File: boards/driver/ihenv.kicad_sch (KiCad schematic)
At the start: 8 parts, among them Q56 MMBT2222, Q57 MMBT2907, Q58 MMBT2222

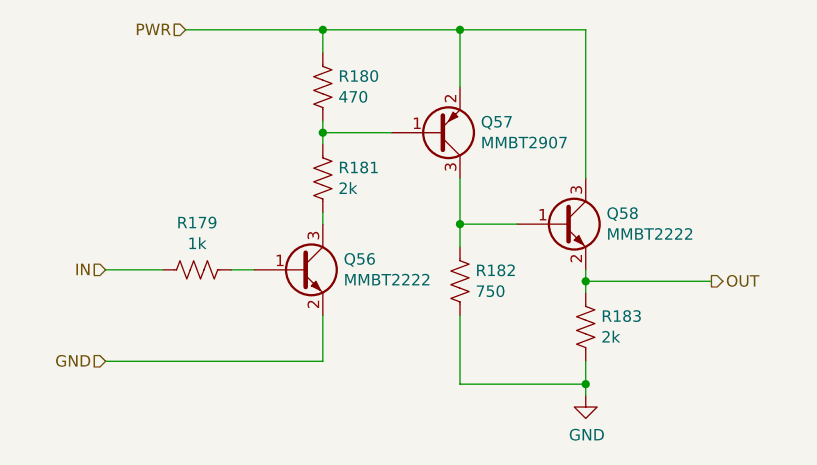
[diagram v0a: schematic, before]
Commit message: Driver: Added a 5V->3.3V LDO to replace the reversed cmod header, added jumpers for the 200R parallel returns, and renamed subcircuit ports to avoid unexpected ground connections.
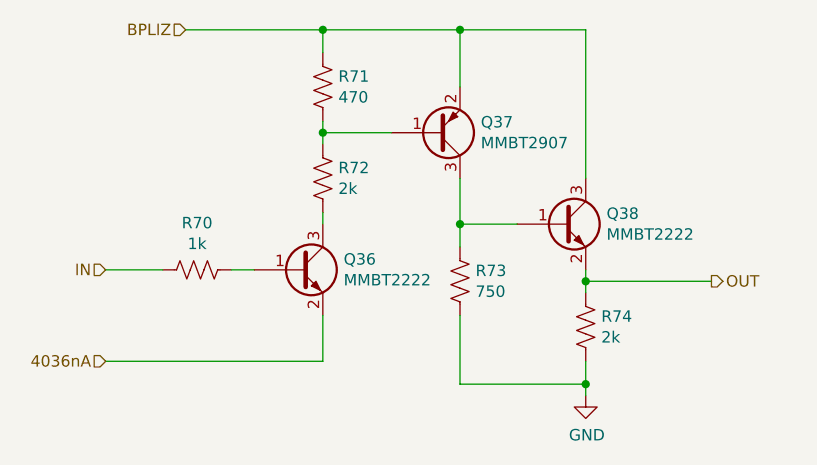
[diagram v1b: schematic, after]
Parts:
- renumbered Q56 to Q36, Q57 to Q37, Q58 to Q38, R179 to R70, R180 to R71, R181 to R72, R182 to R73, R183 to R74
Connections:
- net GND: no longer Q36.2 (E)
- net PWR renamed BPLIZ
- new net 4036nA: Q36.2 (E)
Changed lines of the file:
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@@
     (stroke (width 0) (type default) (color 0 0 0 0))
   )
-  (hierarchical_label "GND" (shape input) (at 90.17 102.87 180)
+  (hierarchical_label "4036nA" (shape input) (at 90.17 102.87 180)
     (effects (font (size 1.27 1.27)) (justify right))
   )
@@
     (effects (font (size 1.27 1.27)) (justify right))
   )
-  (hierarchical_label "PWR" (shape input) (at 99.06 66.04 180)
+  (hierarchical_label "BPLIZ" (shape input) (at 99.06 66.04 180)
     (effects (font (size 1.27 1.27)) (justify right))
   )
   (symbol (lib_id "Device:R_US") (at 100.33 92.71 270)
     (in_bom yes) (on_board yes)
-    (property "Reference" "R179" (id 0) (at 100.33 87.503 90))
+    (property "Reference" "R70" (id 0) (at 100.33 87.503 90))
     (property "Value" "1k" (id 1) (at 100.33 89.8144 90))
     (property "Footprint" "Resistor_SMD:R_0603_1608Metric" (id 2) (at 100.076 93.726 90)
@@
   (symbol (lib_id "Device:Q_NPN_BEC") (at 111.76 92.71 0)
     (in_bom yes) (on_board yes)
-    (property "Reference" "Q56" (id 0) (at 116.6114 91.5416 0)
+    (property "Reference" "Q36" (id 0) (at 116.6114 91.5416 0)
       (effects (font (size 1.27 1.27)) (justify left))
     )
@@
   (symbol (lib_id "Device:Q_PNP_BEC") (at 127 77.47 0) (mirror x)
     (in_bom yes) (on_board yes)
-    (property "Reference" "Q57" (id 0) (at 131.8514 76.3016 0)
+    (property "Reference" "Q37" (id 0) (at 131.8514 76.3016 0)
       (effects (font (size 1.27 1.27)) (justify left))
     )
@@
   (symbol (lib_id "power:GND") (at 143.51 106.68 0)
     (in_bom yes) (on_board yes)
-    (property "Reference" "#PWR097" (id 0) (at 143.51 113.03 0)
+    (property "Reference" "#PWR018" (id 0) (at 143.51 113.03 0)
       (effects (font (size 1.27 1.27)) hide)
     )
@@
   (symbol (lib_id "Device:R_US") (at 114.3 82.55 0)
     (in_bom yes) (on_board yes)
-    (property "Reference" "R181" (id 0) (at 116.0272 81.3816 0)
+    (property "Reference" "R72" (id 0) (at 116.0272 81.3816 0)
       (effects (font (size 1.27 1.27)) (justify left))
     )
@@
   (symbol (lib_id "Device:R_US") (at 114.3 72.39 0)
     (in_bom yes) (on_board yes)
-    (property "Reference" "R180" (id 0) (at 116.0272 71.2216 0)
+    (property "Reference" "R71" (id 0) (at 116.0272 71.2216 0)
       (effects (font (size 1.27 1.27)) (justify left))
     )
@@
   (symbol (lib_id "Device:Q_NPN_BEC") (at 140.97 87.63 0)
     (in_bom yes) (on_board yes)
-    (property "Reference" "Q58" (id 0) (at 145.8214 86.4616 0)
+    (property "Reference" "Q38" (id 0) (at 145.8214 86.4616 0)
       (effects (font (size 1.27 1.27)) (justify left))
     )
@@
   (symbol (lib_id "Device:R_US") (at 129.54 93.98 0)
     (in_bom yes) (on_board yes)
-    (property "Reference" "R182" (id 0) (at 131.2672 92.8116 0)
+    (property "Reference" "R73" (id 0) (at 131.2672 92.8116 0)
       (effects (font (size 1.27 1.27)) (justify left))
     )
@@
   (symbol (lib_id "Device:R_US") (at 143.51 99.06 0)
     (in_bom yes) (on_board yes)
-    (property "Reference" "R183" (id 0) (at 145.2372 97.8916 0)
+    (property "Reference" "R74" (id 0) (at 145.2372 97.8916 0)
       (effects (font (size 1.27 1.27)) (justify left))
     )

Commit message: Driver: incorporated most changes from the test board, and began layout
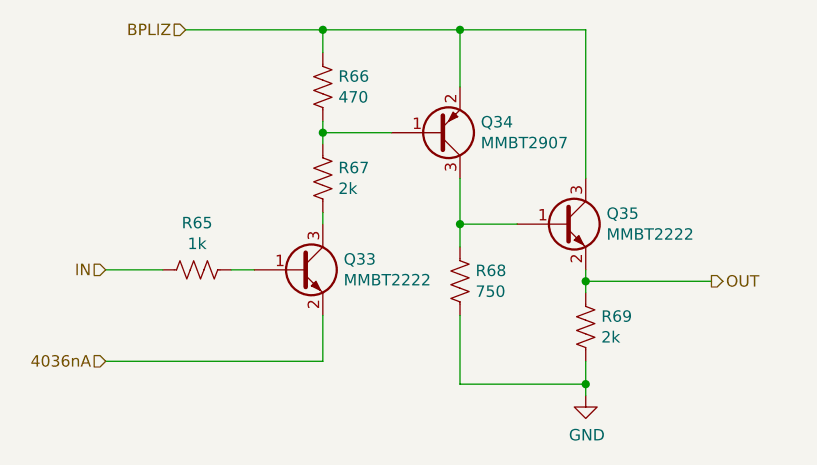
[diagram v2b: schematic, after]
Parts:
- renumbered Q36 to Q33, Q37 to Q34, Q38 to Q35, R70 to R65, R71 to R66, R72 to R67, R73 to R68, R74 to R69
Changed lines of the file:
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@@
     (effects (font (size 1.27 1.27)) (justify right))
   )
-  (symbol (lib_id "Device:R_US") (at 100.33 92.71 270)
+  (symbol (lib_id "Device:R_US") (at 100.33 92.71 270) (unit 1)
     (in_bom yes) (on_board yes)
-    (property "Reference" "R70" (id 0) (at 100.33 87.503 90))
+    (property "Reference" "R65" (id 0) (at 100.33 87.503 90))
     (property "Value" "1k" (id 1) (at 100.33 89.8144 90))
     (property "Footprint" "Resistor_SMD:R_0603_1608Metric" (id 2) (at 100.076 93.726 90)
@@
     (pin "2")
   )
-  (symbol (lib_id "Device:Q_NPN_BEC") (at 111.76 92.71 0)
+  (symbol (lib_id "Device:Q_NPN_BEC") (at 111.76 92.71 0) (unit 1)
     (in_bom yes) (on_board yes)
-    (property "Reference" "Q36" (id 0) (at 116.6114 91.5416 0)
+    (property "Reference" "Q33" (id 0) (at 116.6114 91.5416 0)
       (effects (font (size 1.27 1.27)) (justify left))
     )
@@
     (pin "3")
   )
-  (symbol (lib_id "Device:Q_PNP_BEC") (at 127 77.47 0) (mirror x)
+  (symbol (lib_id "Device:Q_PNP_BEC") (at 127 77.47 0) (mirror x) (unit 1)
     (in_bom yes) (on_board yes)
-    (property "Reference" "Q37" (id 0) (at 131.8514 76.3016 0)
+    (property "Reference" "Q34" (id 0) (at 131.8514 76.3016 0)
       (effects (font (size 1.27 1.27)) (justify left))
     )
@@
     (pin "3")
   )
-  (symbol (lib_id "power:GND") (at 143.51 106.68 0)
+  (symbol (lib_id "power:GND") (at 143.51 106.68 0) (unit 1)
     (in_bom yes) (on_board yes)
-    (property "Reference" "#PWR018" (id 0) (at 143.51 113.03 0)
+    (property "Reference" "#PWR017" (id 0) (at 143.51 113.03 0)
       (effects (font (size 1.27 1.27)) hide)
     )
@@
     (pin "1")
   )
-  (symbol (lib_id "Device:R_US") (at 114.3 82.55 0)
+  (symbol (lib_id "Device:R_US") (at 114.3 82.55 0) (unit 1)
     (in_bom yes) (on_board yes)
-    (property "Reference" "R72" (id 0) (at 116.0272 81.3816 0)
+    (property "Reference" "R67" (id 0) (at 116.0272 81.3816 0)
       (effects (font (size 1.27 1.27)) (justify left))
     )
@@
     (pin "2")
   )
-  (symbol (lib_id "Device:R_US") (at 114.3 72.39 0)
+  (symbol (lib_id "Device:R_US") (at 114.3 72.39 0) (unit 1)
     (in_bom yes) (on_board yes)
-    (property "Reference" "R71" (id 0) (at 116.0272 71.2216 0)
+    (property "Reference" "R66" (id 0) (at 116.0272 71.2216 0)
       (effects (font (size 1.27 1.27)) (justify left))
     )
@@
     (pin "2")
   )
-  (symbol (lib_id "Device:Q_NPN_BEC") (at 140.97 87.63 0)
+  (symbol (lib_id "Device:Q_NPN_BEC") (at 140.97 87.63 0) (unit 1)
     (in_bom yes) (on_board yes)
-    (property "Reference" "Q38" (id 0) (at 145.8214 86.4616 0)
+    (property "Reference" "Q35" (id 0) (at 145.8214 86.4616 0)
       (effects (font (size 1.27 1.27)) (justify left))
     )
@@
     (pin "3")
   )
-  (symbol (lib_id "Device:R_US") (at 129.54 93.98 0)
+  (symbol (lib_id "Device:R_US") (at 129.54 93.98 0) (unit 1)
     (in_bom yes) (on_board yes)
-    (property "Reference" "R73" (id 0) (at 131.2672 92.8116 0)
+    (property "Reference" "R68" (id 0) (at 131.2672 92.8116 0)
       (effects (font (size 1.27 1.27)) (justify left))
     )
@@
     (pin "2")
   )
-  (symbol (lib_id "Device:R_US") (at 143.51 99.06 0)
+  (symbol (lib_id "Device:R_US") (at 143.51 99.06 0) (unit 1)
     (in_bom yes) (on_board yes)
-    (property "Reference" "R74" (id 0) (at 145.2372 97.8916 0)
+    (property "Reference" "R69" (id 0) (at 145.2372 97.8916 0)
       (effects (font (size 1.27 1.27)) (justify left))
     )

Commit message: Driver: progress on subcircuit layout and overall placement
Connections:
- net IN renamed IHENV
- net OUT renamed 4033nA
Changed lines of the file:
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@@
     (effects (font (size 1.27 1.27)) (justify right))
   )
-  (hierarchical_label "OUT" (shape output) (at 157.48 93.98 0)
+  (hierarchical_label "4033nA" (shape output) (at 157.48 93.98 0)
     (effects (font (size 1.27 1.27)) (justify left))
   )
-  (hierarchical_label "IN" (shape input) (at 90.17 92.71 180)
+  (hierarchical_label "IHENV" (shape input) (at 90.17 92.71 180)
     (effects (font (size 1.27 1.27)) (justify right))
   )

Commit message: Driver: minor schematic cleanup and populated all of the BOM except for resistors
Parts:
- Q33, Q35: MPN (none) -> MMBT2222ALT1HTSA1; Manufacturer (none) -> Infineon Technologies; Package (none) -> SOT-23-3
- Q34: MPN (none) -> MMBT2907ALT1HTSA1; Manufacturer (none) -> Infineon Technologies; Package (none) -> SOT-23-3
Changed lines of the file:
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@@
+      (effects (font (size 1.27 1.27)) hide)
+    )
+    (property "MPN" "MMBT2222ALT1HTSA1" (id 6) (at 111.76 92.71 0)
+      (effects (font (size 1.27 1.27)) hide)
+    )
+    (property "Manufacturer" "Infineon Technologies" (id 7) (at 111.76 92.71 0)
+      (effects (font (size 1.27 1.27)) hide)
+    )
+    (property "Description" "TRANS NPN 40V 0.6A SOT-23" (id 8) (at 111.76 92.71 0)
+      (effects (font (size 1.27 1.27)) hide)
+    )
+    (property "Package" "SOT-23-3" (id 9) (at 111.76 92.71 0)
       (effects (font (size 1.27 1.27)) hide)
     )
@@
     )
     (property "Part Number" "MMBT2907A-G" (id 5) (at 127 77.47 0)
+      (effects (font (size 1.27 1.27)) hide)
+    )
+    (property "MPN" "MMBT2907ALT1HTSA1" (id 6) (at 127 77.47 0)
+      (effects (font (size 1.27 1.27)) hide)
+    )
+    (property "Manufacturer" "Infineon Technologies" (id 7) (at 127 77.47 0)
+      (effects (font (size 1.27 1.27)) hide)
+    )
+    (property "Description" "TRANS PNP 60V 0.6A SOT23" (id 8) (at 127 77.47 0)
+      (effects (font (size 1.27 1.27)) hide)
+    )
+    (property "Package" "SOT-23-3" (id 9) (at 127 77.47 0)
       (effects (font (size 1.27 1.27)) hide)
     )
@@
       (effects (font (size 1.27 1.27)) hide)
     )
+    (property "MPN" "MMBT2222ALT1HTSA1" (id 6) (at 140.97 87.63 0)
+      (effects (font (size 1.27 1.27)) hide)
+    )
+    (property "Manufacturer" "Infineon Technologies" (id 7) (at 140.97 87.63 0)
+      (effects (font (size 1.27 1.27)) hide)
+    )
+    (property "Description" "TRANS NPN 40V 0.6A SOT-23" (id 8) (at 140.97 87.63 0)
+      (effects (font (size 1.27 1.27)) hide)
+    )
+    (property "Package" "SOT-23-3" (id 9) (at 140.97 87.63 0)
+      (effects (font (size 1.27 1.27)) hide)
+    )

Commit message: Driver: filled out the rest of the BOM, except for defaults for nominal resistances
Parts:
- R65: MPN (none) -> ESR03EZPF1001; Manufacturer (none) -> Rohm Semiconductor; Package (none) -> 0603; Rating (none) -> 1/4W; Tolerance (none) -> 1%
- R66: MPN (none) -> RMCF0603FT470R; Manufacturer (none) -> Stackpole Electronics Inc; Package (none) -> 0603; Rating (none) -> 1/10W; Tolerance (none) -> 1%
- R67, R69: MPN (none) -> ERJ-PA3F2001V; Manufacturer (none) -> Panasonic Electronic Components; Package (none) -> 0603; Rating (none) -> 1/3W; Tolerance (none) -> 1%
- R68: MPN (none) -> RMCF0603FT750R; Manufacturer (none) -> Stackpole Electronics Inc; Package (none) -> 0603; Rating (none) -> 1/10W; Tolerance (none) -> 1%
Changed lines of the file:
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@@
+      (effects (font (size 1.27 1.27)) hide)
+    )
+    (property "Description" "RES SMD 1K OHM PULSE-WITHSTANDING 1% 1/4W 0603" (id 4) (at 100.33 92.71 0)
+      (effects (font (size 1.27 1.27)) hide)
+    )
+    (property "MPN" "ESR03EZPF1001" (id 5) (at 100.33 92.71 0)
+      (effects (font (size 1.27 1.27)) hide)
+    )
+    (property "Manufacturer" "Rohm Semiconductor" (id 6) (at 100.33 92.71 0)
+      (effects (font (size 1.27 1.27)) hide)
+    )
+    (property "Package" "0603" (id 7) (at 100.33 92.71 0)
+      (effects (font (size 1.27 1.27)) hide)
+    )
+    (property "Rating" "1/4W" (id 8) (at 100.33 92.71 0)
+      (effects (font (size 1.27 1.27)) hide)
+    )
+    (property "Tolerance" "1%" (id 9) (at 100.33 92.71 0)
       (effects (font (size 1.27 1.27)) hide)
     )
@@
       (effects (font (size 1.27 1.27)) hide)
     )
+    (property "Description" "RES SMD 2K OHM PULSE-WITHSTANDING 1% 1/3W 0603" (id 4) (at 114.3 82.55 0)
+      (effects (font (size 1.27 1.27)) hide)
+    )
+    (property "MPN" "ERJ-PA3F2001V" (id 5) (at 114.3 82.55 0)
+      (effects (font (size 1.27 1.27)) hide)
+    )
+    (property "Manufacturer" "Panasonic Electronic Components" (id 6) (at 114.3 82.55 0)
+      (effects (font (size 1.27 1.27)) hide)
+    )
+    (property "Package" "0603" (id 7) (at 114.3 82.55 0)
+      (effects (font (size 1.27 1.27)) hide)
+    )
+    (property "Rating" "1/3W" (id 8) (at 114.3 82.55 0)
+      (effects (font (size 1.27 1.27)) hide)
+    )
+    (property "Tolerance" "1%" (id 9) (at 114.3 82.55 0)
+      (effects (font (size 1.27 1.27)) hide)
+    )
     (pin "1")
     (pin "2")
@@
       (effects (font (size 1.27 1.27)) hide)
     )
+    (property "Description" "RES 470 OHM 1% 1/10W 0603" (id 4) (at 114.3 72.39 0)
+      (effects (font (size 1.27 1.27)) hide)
+    )
+    (property "MPN" "RMCF0603FT470R" (id 5) (at 114.3 72.39 0)
+      (effects (font (size 1.27 1.27)) hide)
+    )
+    (property "Manufacturer" "Stackpole Electronics Inc" (id 6) (at 114.3 72.39 0)
+      (effects (font (size 1.27 1.27)) hide)
+    )
+    (property "Package" "0603" (id 7) (at 114.3 72.39 0)
+      (effects (font (size 1.27 1.27)) hide)
+    )
+    (property "Rating" "1/10W" (id 8) (at 114.3 72.39 0)
+      (effects (font (size 1.27 1.27)) hide)
+    )
+    (property "Tolerance" "1%" (id 9) (at 114.3 72.39 0)
+      (effects (font (size 1.27 1.27)) hide)
+    )
     (pin "1")
     (pin "2")
@@
       (effects (font (size 1.27 1.27)) hide)
     )
+    (property "Description" "RES 750 OHM 1% 1/10W 0603" (id 4) (at 129.54 93.98 0)
+      (effects (font (size 1.27 1.27)) hide)
+    )
+    (property "MPN" "RMCF0603FT750R" (id 5) (at 129.54 93.98 0)
+      (effects (font (size 1.27 1.27)) hide)
+    )
+    (property "Manufacturer" "Stackpole Electronics Inc" (id 6) (at 129.54 93.98 0)
+      (effects (font (size 1.27 1.27)) hide)
+    )
+    (property "Package" "0603" (id 7) (at 129.54 93.98 0)
+      (effects (font (size 1.27 1.27)) hide)
+    )
+    (property "Rating" "1/10W" (id 8) (at 129.54 93.98 0)
+      (effects (font (size 1.27 1.27)) hide)
+    )
+    (property "Tolerance" "1%" (id 9) (at 129.54 93.98 0)
+      (effects (font (size 1.27 1.27)) hide)
+    )
     (pin "1")
     (pin "2")
@@
       (effects (font (size 1.27 1.27)) hide)
     )
+    (property "Description" "RES SMD 2K OHM PULSE-WITHSTANDING 1% 1/3W 0603" (id 4) (at 143.51 99.06 0)
+      (effects (font (size 1.27 1.27)) hide)
+    )
+    (property "MPN" "ERJ-PA3F2001V" (id 5) (at 143.51 99.06 0)
+      (effects (font (size 1.27 1.27)) hide)
+    )
+    (property "Manufacturer" "Panasonic Electronic Components" (id 6) (at 143.51 99.06 0)
+      (effects (font (size 1.27 1.27)) hide)
+    )
+    (property "Package" "0603" (id 7) (at 143.51 99.06 0)
+      (effects (font (size 1.27 1.27)) hide)
+    )
+    (property "Rating" "1/3W" (id 8) (at 143.51 99.06 0)
+      (effects (font (size 1.27 1.27)) hide)
+    )
+    (property "Tolerance" "1%" (id 9) (at 143.51 99.06 0)
+      (effects (font (size 1.27 1.27)) hide)
+    )
